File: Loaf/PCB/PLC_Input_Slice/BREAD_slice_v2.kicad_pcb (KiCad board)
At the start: 2 copper layers, 100 x 70.6 mm, 34 parts, among them J1 10018783-10200TLF, J2 Barrel Jack, J3 DB25_Socket, U1 MCP4922-EP, U2 MCP4922-EP, U3 MCP4922-EP, U4 MCP4922-EP, U5 MCP3208, U6 MCP2561-E-P, U7 MCP2515-xSO, Y1 16MHZ Crystal

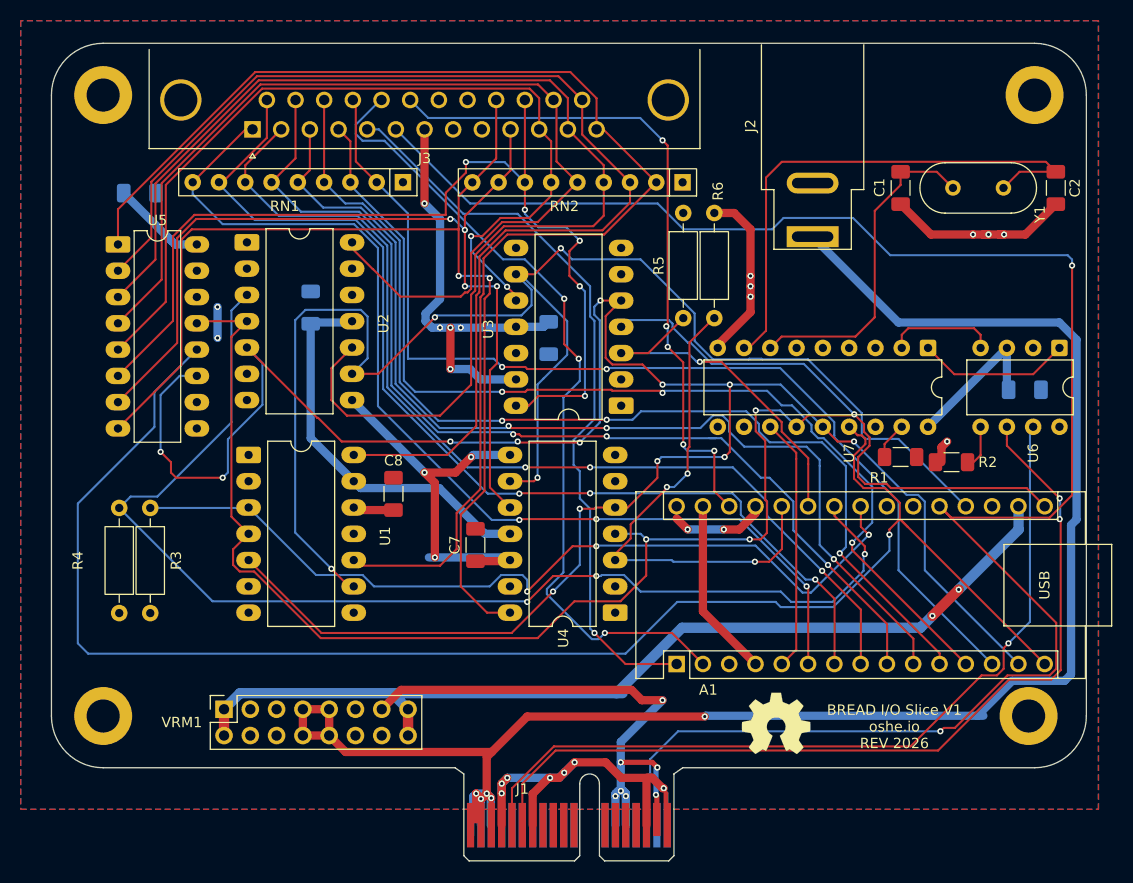
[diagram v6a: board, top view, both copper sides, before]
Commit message: Fixed the I/O PCB because the routing was noisy
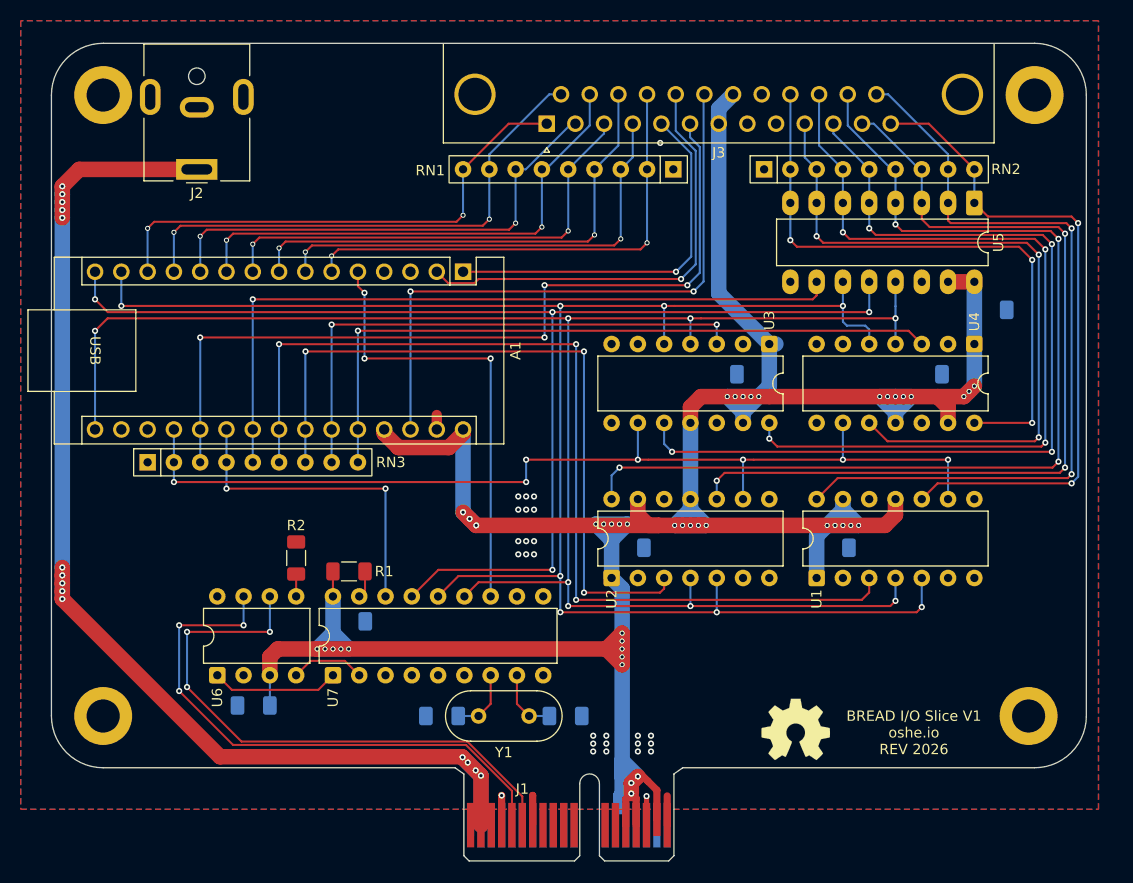
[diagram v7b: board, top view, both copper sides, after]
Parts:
- removed R3, R4, R5, R6: 10k, Resistor_THT:R_Axial_DIN0207_L6.3mm_D2.5mm_P10.16mm_Horizontal
- removed VRM1: Optional VRM, Connector_PinSocket_2.54mm:PinSocket_2x08_P2.54mm_Vertical
- added C9: 0.47uF, Capacitor_SMD:C_1206_3216Metric_Pad1.33x1.80mm_HandSolder, B.Cu at (130.2, 111.4)
- added RN3: 10K Resistor Array, Resistor_THT:R_Array_SIP9, F.Cu at (110.7, 96.0)
- C1, C2, C7, C8: moved to B.Cu
- J2: value Barrel Jack -> Barrel_Jack; footprint Connector_BarrelJack:BarrelJack_SwitchcraftConxall_RAPC10U_Horizontal -> Connector_BarrelJack:BarrelJack_CUI_PJ-063AH_Horizontal
- U1, U2, U3, U4: footprint Package_DIP:DIP-14_W10.16mm_LongPads -> Package_DIP:DIP-14_W7.62mm
- moved U6 87.3 mm to (117.5, 116.6), turned to 90 degrees
- moved U5 82.8 mm to (190.6, 71.0), turned to -90 degrees
- moved C2 69.6 mm to (151.1, 120.5), turned to 0 degrees
- moved Y1 68.6 mm to (147.6, 120.5)
- moved C1 67.6 mm to (139.2, 120.5), turned to 180 degrees
- moved U7 65.6 mm to (128.7, 116.6), turned to 90 degrees
- moved R2 64.0 mm to (125.1, 105.3), turned to -90 degrees
- moved J2 59.9 mm to (115.5, 67.7), turned to 180 degrees
- moved C4 58.3 mm to (157.1, 104.3)
- moved U1 56.2 mm to (175.4, 107.2), turned to 90 degrees
- moved C7 54.7 mm to (192.2, 81.3), turned to 180 degrees
- moved R1 54.4 mm to (130.2, 106.6), turned to 180 degrees
- moved U2 47.9 mm to (155.6, 107.2), turned to 90 degrees
- moved U4 43.3 mm to (190.6, 84.6), turned to -90 degrees
- moved C5 43.2 mm to (169.3, 87.5), turned to 0 degrees
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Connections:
- A1 pad 10: /DIO4 -> /DIO3
- A1 pad 11: /DIO5 -> /DIO2
- A1 pad 12: /DIO6 -> /DIO1
- A1 pad 13: /DIO7 -> /DIO0
- A1 pad 21: unconnected-(A1-A2-Pad21) -> /CAN_CS
- A1 pad 22: unconnected-(A1-A3-Pad22) -> /CS1
- A1 pad 6: /DIO0 -> /DIO7
- A1 pad 7: /DIO1 -> /DIO6
- A1 pad 8: /DIO2 -> /DIO5
- A1 pad 9: /DIO3 -> /DIO4
- J1 pad A16: /ESTOP -> /EstpCh1
- RN2 pad 2: /AIO0 -> /AIO7
- RN2 pad 3: /AIO1 -> /AIO6
- RN2 pad 4: /AIO2 -> /AIO5
- RN2 pad 5: /AIO3 -> /AIO4
- RN2 pad 6: /AIO4 -> /AIO3
- RN2 pad 7: /AIO5 -> /AIO2
- RN2 pad 8: /AIO6 -> /AIO1
- RN2 pad 9: /AIO7 -> /AIO0
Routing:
- net +5V: track 174.8 -> 309.4 mm, vias 16 -> 44
- net GND: track 141.9 -> 12.8 mm, vias 17 -> 27
- net /ESTOP: track 178.1 -> 80.6 mm, vias 2 -> 4
- net +3.3V: track 94.1 -> 0.00 mm, vias 2 -> 0
- net /CS1: track 0.00 -> 71.7 mm, vias 0 -> 1
- net /AIO0: track 126.8 -> 64.5 mm, vias 0 -> 2
- net /DIO6: track 99.6 -> 44.5 mm, vias 3 -> 2
- net /DIO4: track 100.3 -> 45.5 mm, vias 3 -> 2
- net /DIO5: track 102.3 -> 47.8 mm, vias 3 -> 2
- net /DIO7: track 100.8 -> 46.9 mm
- net /SHDN: track 150.6 -> 96.8 mm, vias 4 -> 7
- net +12V: track 172.3 -> 119.3 mm, vias 5 -> 14
- net /DIO3: track 100.2 -> 49.0 mm, vias 3 -> 2
- net /DIO0: track 100.7 -> 49.5 mm, vias 3 -> 2
- net /DIO1: track 101.4 -> 50.4 mm, vias 3 -> 2
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- added copper zone on F.Cu, net GND
- removed copper zone on F.Cu, net +5V

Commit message: Fixed nano placement
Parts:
- moved A1 2.54 mm to (143.8, 77.6)
- moved RN3 2.54 mm to (113.3, 96.0)
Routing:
- net /CANH: track 54.8 -> 59.2 mm
- net /CANL: track 56.3 -> 59.2 mm
- net /SHDN: track 96.8 -> 94.2 mm
- net /DAC4: track 67.7 -> 65.2 mm
- net /UTX: track 36.7 -> 34.1 mm
- net /ESTOP: track 80.6 -> 78.0 mm
- net /DIO4: track 45.5 -> 42.9 mm
- net /DIO2: track 47.2 -> 44.7 mm
- net /DIO0: track 49.5 -> 47.0 mm
- net /DAC2: track 69.9 -> 67.3 mm
- net /CS1: track 71.7 -> 69.2 mm
- net /URX: track 43.5 -> 40.9 mm
- net /DIO6: track 44.5 -> 42.0 mm
- net /DIO5: track 47.8 -> 45.3 mm
- net /DIO3: track 49.0 -> 46.5 mm
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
